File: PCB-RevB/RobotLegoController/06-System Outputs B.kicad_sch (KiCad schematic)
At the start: 113 parts

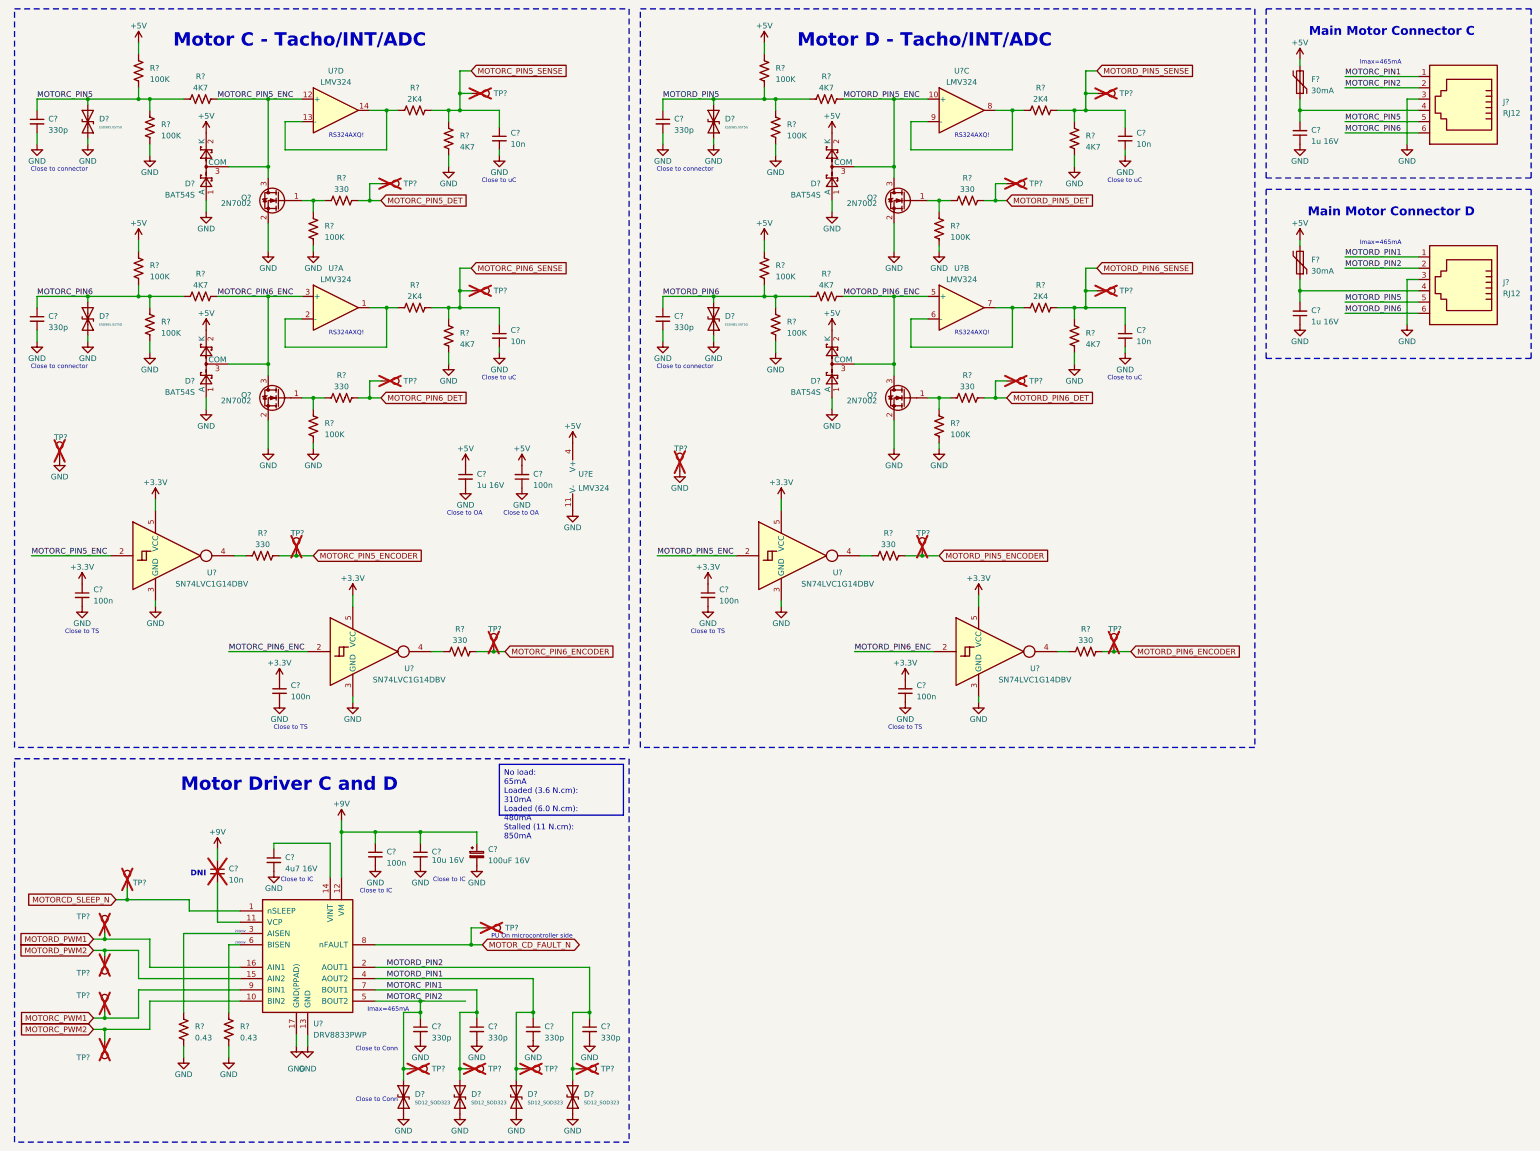
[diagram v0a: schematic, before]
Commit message: Finish updating schematic REV B
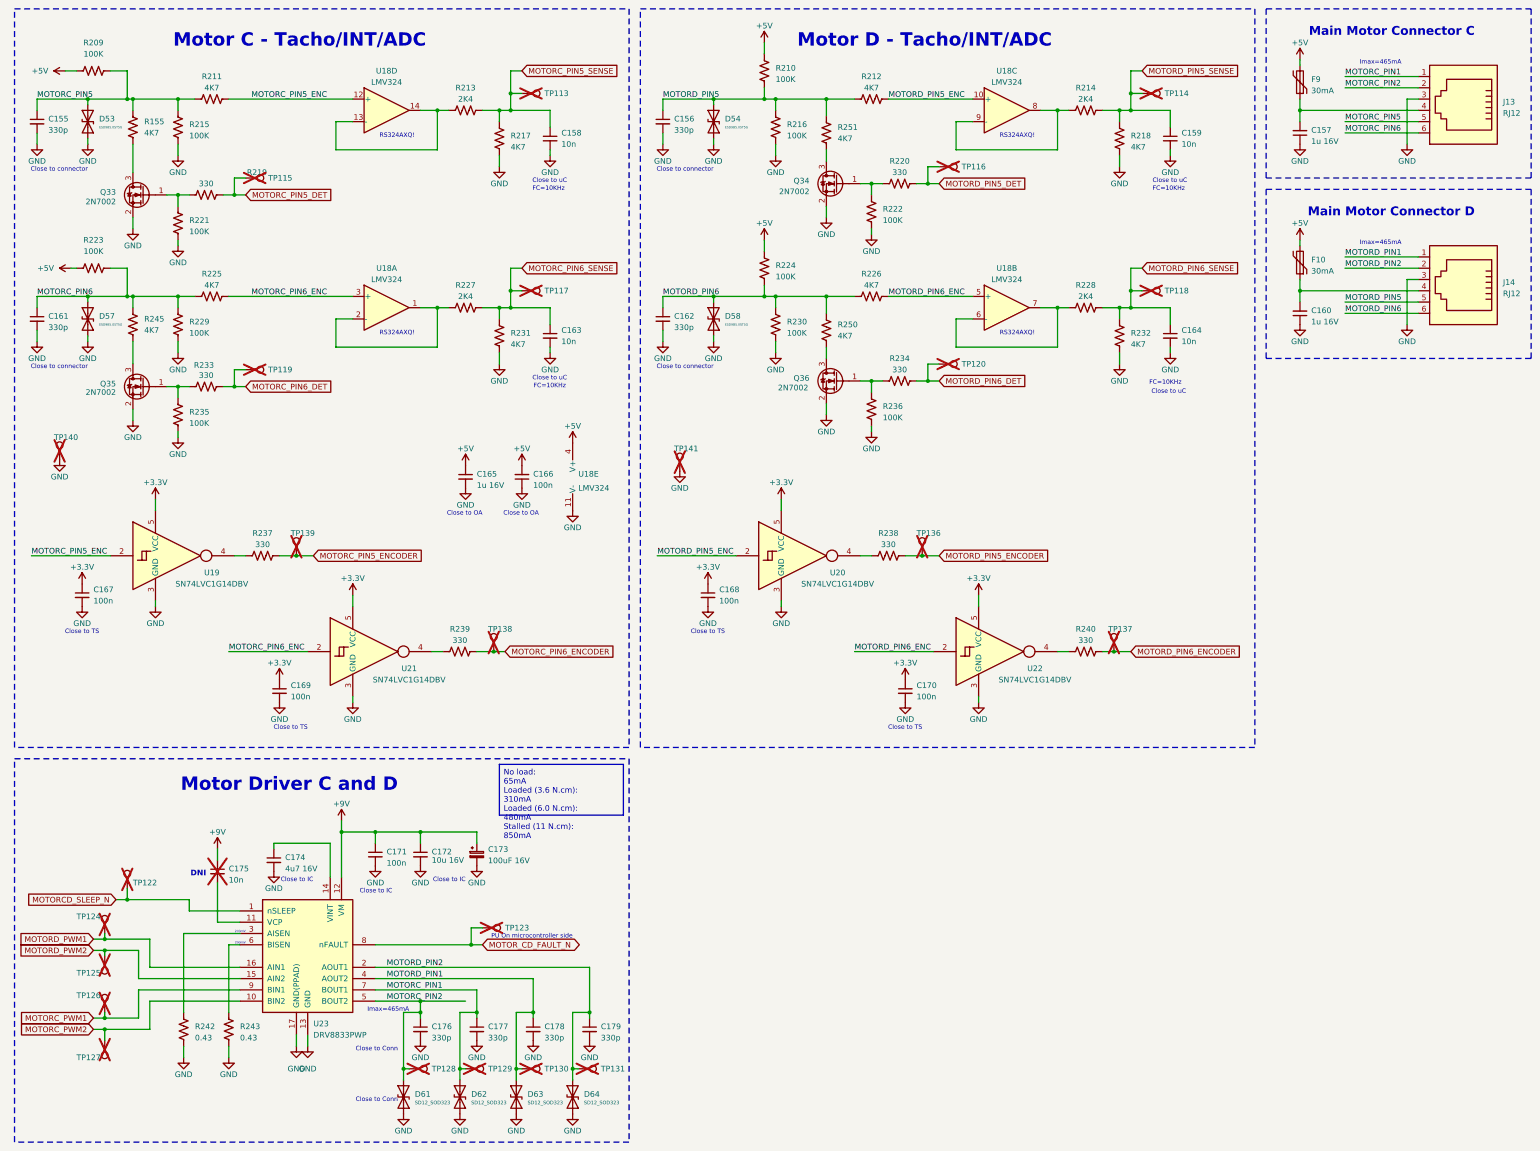
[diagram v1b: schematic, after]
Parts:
- removed D? (x4): BAT54S, Package_TO_SOT_SMD:SOT-23, symbol Diode:BAT54S
- added R155, R245, R250, R251: 4K7, Resistor_SMD:R_0402_1005Metric, symbol Device:R_US
- J13, J14: renamed from J?; footprint Connector_RJ:RJ12_Amphenol_54601 -> Connector_RJ:RJ25_Wayconn_MJEA-660X1_Horizontal
- gave numbers to parts that had none: 103
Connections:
- net MOTORC_PIN5: now also R155.1
- net MOTORC_PIN5_ENC: no longer Q33.3 (D)
- net MOTORC_PIN6: now also R245.1
- net MOTORC_PIN6_ENC: no longer Q35.3 (D)
- net MOTORD_PIN5: now also R251.1
- net MOTORD_PIN5_ENC: no longer Q34.3 (D)
- net MOTORD_PIN6: now also R250.1
- net MOTORD_PIN6_ENC: no longer Q36.3 (D)
- new net: Q34.3 (D), R251.2
- new net: Q36.3 (D), R250.2
- new net: Q33.3 (D), R155.2
- new net: Q35.3 (D), R245.2
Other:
- note added: "FC=10KHz"
- moved on the sheet: C158, C159, C163, C164, Q33, Q34, Q35, Q36, R209, R211, R212, R213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
